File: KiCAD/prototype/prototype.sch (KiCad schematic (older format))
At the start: 0 parts

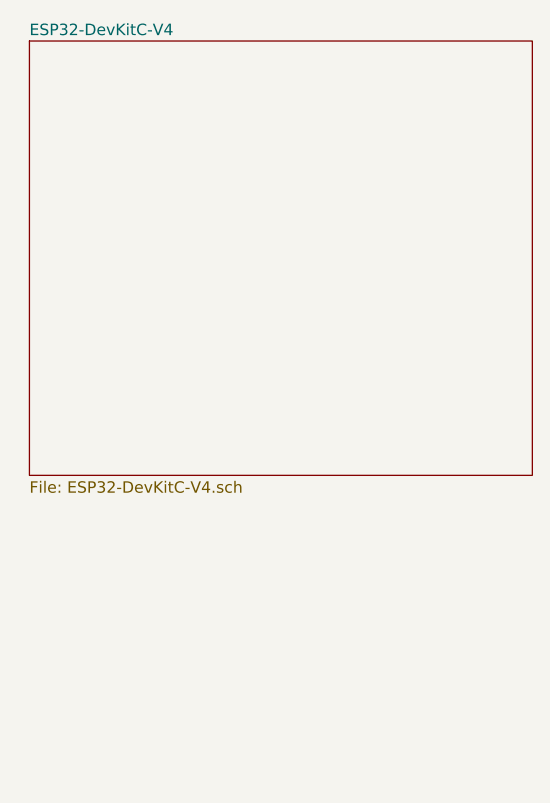
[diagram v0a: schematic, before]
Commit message: Export all signals to the schematic reference
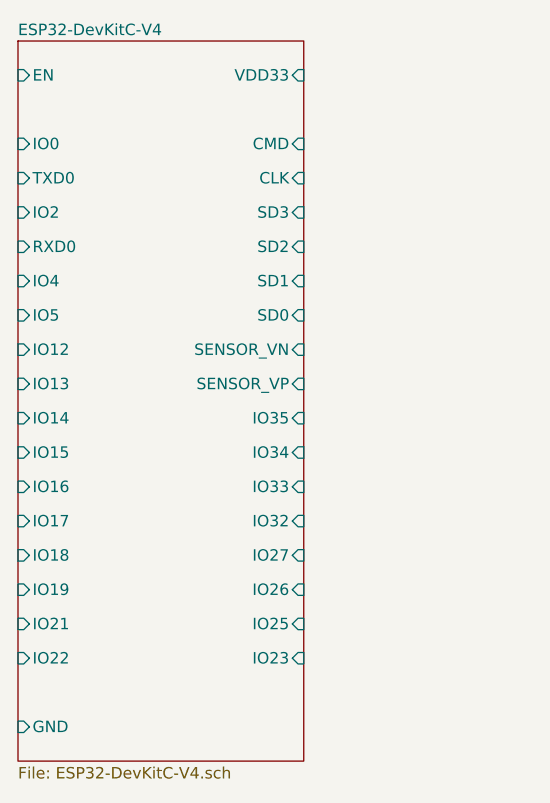
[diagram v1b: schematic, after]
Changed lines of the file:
@@
 $EndDescr
 $Sheet
-S 5150 2800 2200 1900
+S 5100 2800 1250 3150
 U 5F928E95
 F0 "ESP32-DevKitC-V4" 50
 F1 "ESP32-DevKitC-V4.sch" 50
+F2 "IO0" I L 5100 3250 50
+F3 "TXD0" I L 5100 3400 50
+F4 "IO2" I L 5100 3550 50
+F5 "RXD0" I L 5100 3700 50
+F6 "IO4" I L 5100 3850 50
+F7 "IO5" I L 5100 4000 50
+F8 "IO12" I L 5100 4150 50
+F9 "IO13" I L 5100 4300 50
+F10 "IO14" I L 5100 4450 50
+F11 "IO15" I L 5100 4600 50
+F12 "IO16" I L 5100 4750 50
+F13 "IO17" I L 5100 4900 50
+F14 "IO18" I L 5100 5050 50
+F15 "IO19" I L 5100 5200 50
+F16 "IO21" I L 5100 5350 50
+F17 "IO22" I L 5100 5500 50
+F18 "IO23" I R 6350 5500 50
+F19 "IO25" I R 6350 5350 50
+F20 "IO26" I R 6350 5200 50
+F21 "IO27" I R 6350 5050 50
+F22 "IO32" I R 6350 4900 50
+F23 "IO33" I R 6350 4750 50
+F24 "IO34" I R 6350 4600 50
+F25 "IO35" I R 6350 4450 50
+F26 "SENSOR_VP" I R 6350 4300 50
+F27 "SENSOR_VN" I R 6350 4150 50
+F28 "SD0" I R 6350 4000 50
+F29 "SD1" I R 6350 3850 50
+F30 "SD2" I R 6350 3700 50
+F31 "SD3" I R 6350 3550 50
+F32 "CLK" I R 6350 3400 50
+F33 "CMD" I R 6350 3250 50
+F34 "EN" I L 5100 2950 50
+F35 "VDD33" I R 6350 2950 50
+F36 "GND" I L 5100 5800 50
 $EndSheet
 $EndSCHEMATC

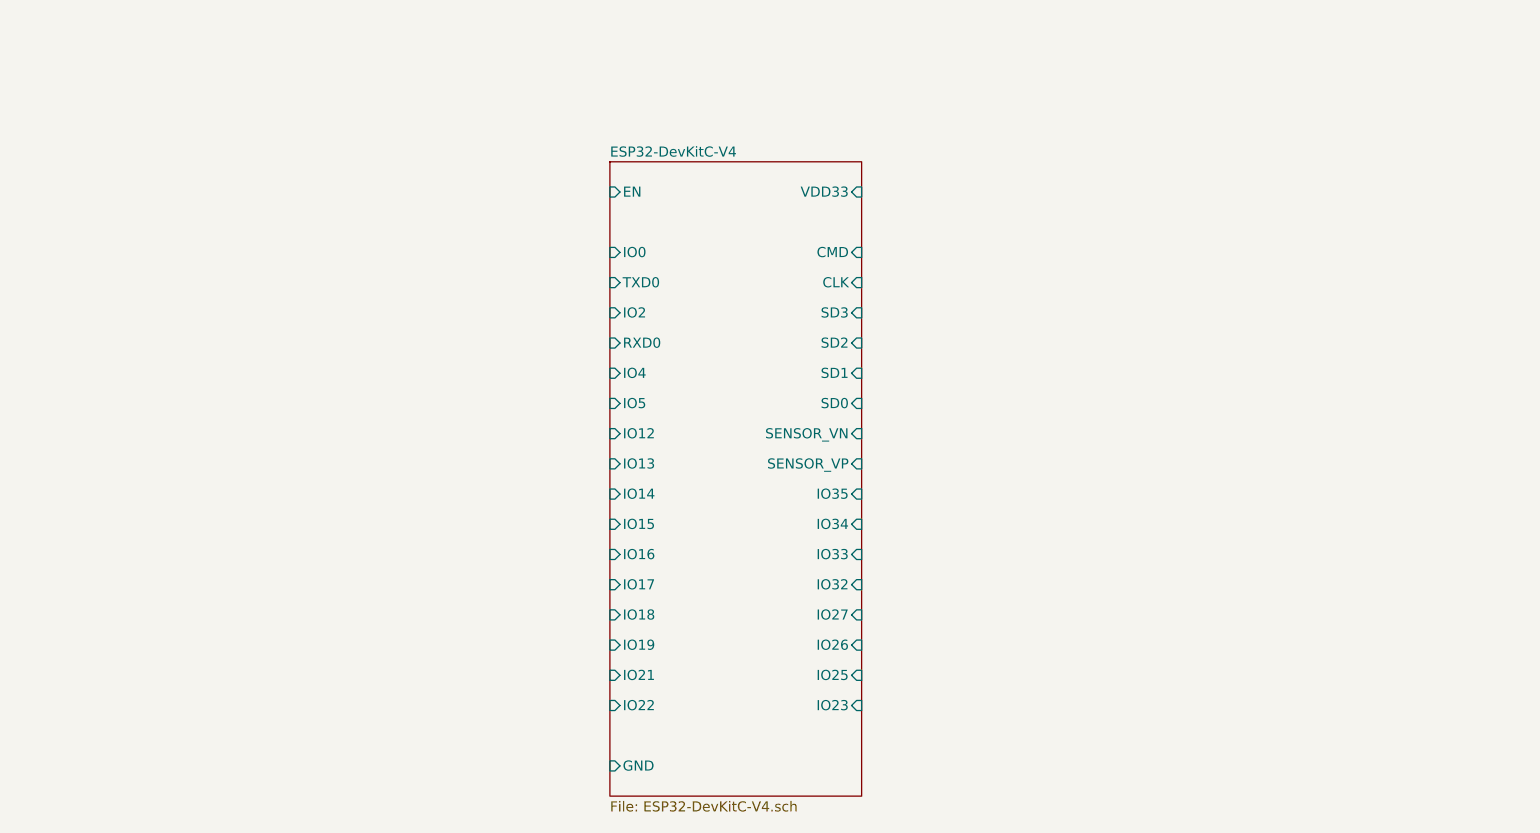
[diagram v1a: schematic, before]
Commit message: Correction of miss placed folder
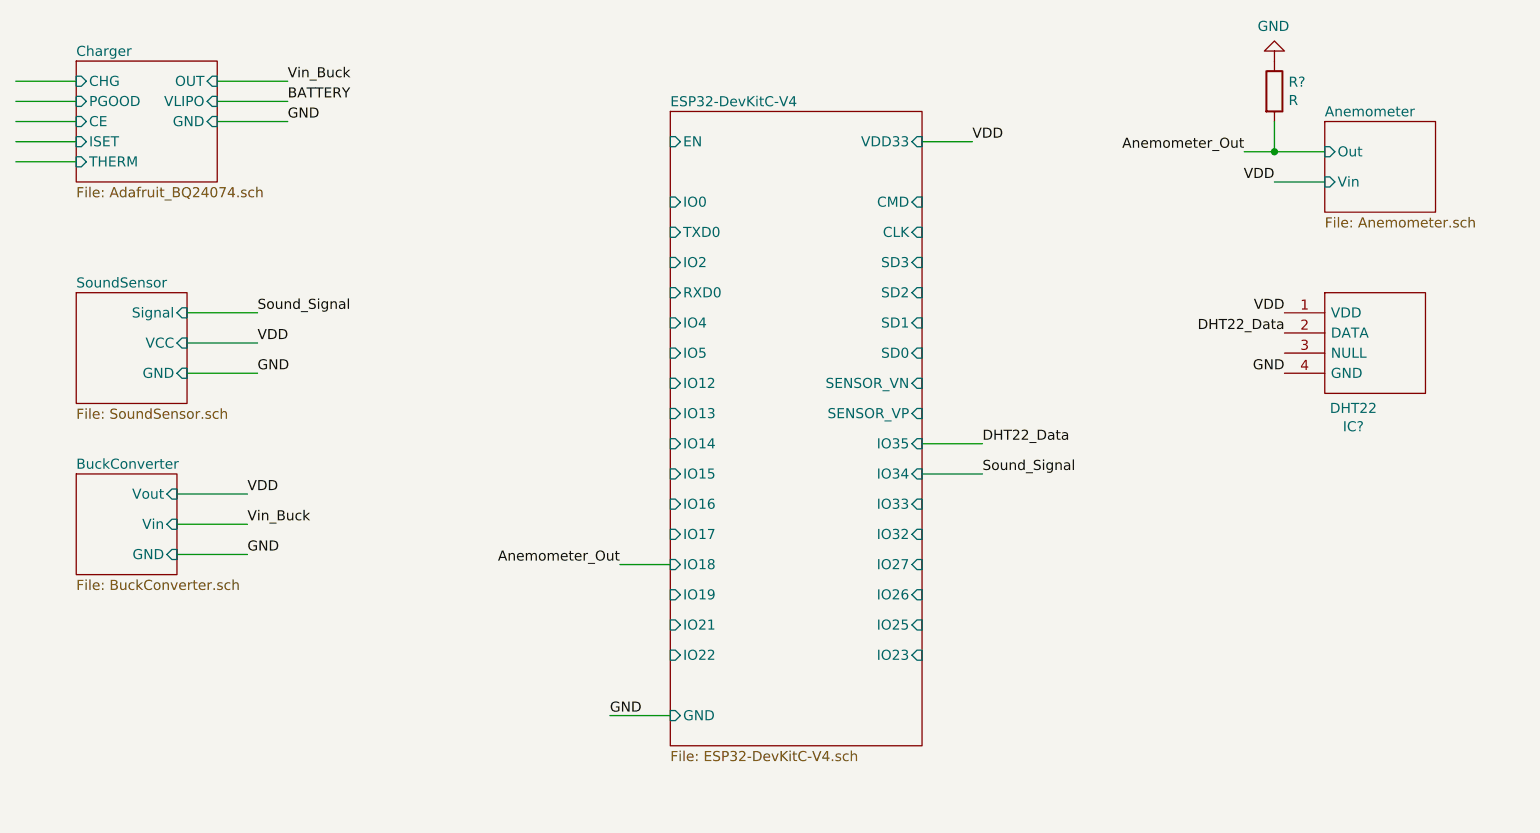
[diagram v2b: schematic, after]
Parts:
- added IC?: DHT22, DHT22, symbol DHT22:DHT22
- added R?: R, symbol Device:R
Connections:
- net labels added: Anemometer_Out, BATTERY, DHT22_Data, GND, Sound_Signal, VDD, Vin_Buck
- wire segments 0 -> 23
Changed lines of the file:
@@
 $Descr A4 11693 8268
 encoding utf-8
-Sheet 1 2
+Sheet 1 6
 Title "Software testing prototype schematics"
 Date "2020-10-22"
@@
 $EndDescr
 $Sheet
-S 5100 2800 1250 3150
+S 5400 2550 1250 3150
 U 5F928E95
 F0 "ESP32-DevKitC-V4" 50
 F1 "ESP32-DevKitC-V4.sch" 50
-F2 "IO0" I L 5100 3250 50
-F3 "TXD0" I L 5100 3400 50
-F4 "IO2" I L 5100 3550 50
-F5 "RXD0" I L 5100 3700 50
-F6 "IO4" I L 5100 3850 50
-F7 "IO5" I L 5100 4000 50
-F8 "IO12" I L 5100 4150 50
-F9 "IO13" I L 5100 4300 50
-F10 "IO14" I L 5100 4450 50
-F11 "IO15" I L 5100 4600 50
-F12 "IO16" I L 5100 4750 50
-F13 "IO17" I L 5100 4900 50
-F14 "IO18" I L 5100 5050 50
-F15 "IO19" I L 5100 5200 50
-F16 "IO21" I L 5100 5350 50
-F17 "IO22" I L 5100 5500 50
-F18 "IO23" I R 6350 5500 50
-F19 "IO25" I R 6350 5350 50
-F20 "IO26" I R 6350 5200 50
-F21 "IO27" I R 6350 5050 50
-F22 "IO32" I R 6350 4900 50
-F23 "IO33" I R 6350 4750 50
-F24 "IO34" I R 6350 4600 50
-F25 "IO35" I R 6350 4450 50
-F26 "SENSOR_VP" I R 6350 4300 50
-F27 "SENSOR_VN" I R 6350 4150 50
-F28 "SD0" I R 6350 4000 50
-F29 "SD1" I R 6350 3850 50
-F30 "SD2" I R 6350 3700 50
-F31 "SD3" I R 6350 3550 50
-F32 "CLK" I R 6350 3400 50
-F33 "CMD" I R 6350 3250 50
-F34 "EN" I L 5100 2950 50
-F35 "VDD33" I R 6350 2950 50
-F36 "GND" I L 5100 5800 50
-$EndSheet
+F2 "IO0" I L 5400 3000 50
+F3 "TXD0" I L 5400 3150 50
+F4 "IO2" I L 5400 3300 50
+F5 "RXD0" I L 5400 3450 50
+F6 "IO4" I L 5400 3600 50
+F7 "IO5" I L 5400 3750 50
+F8 "IO12" I L 5400 3900 50
+F9 "IO13" I L 5400 4050 50
+F10 "IO14" I L 5400 4200 50
+F11 "IO15" I L 5400 4350 50
+F12 "IO16" I L 5400 4500 50
+F13 "IO17" I L 5400 4650 50
+F14 "IO18" I L 5400 4800 50
+F15 "IO19" I L 5400 4950 50
+F16 "IO21" I L 5400 5100 50
+F17 "IO22" I L 5400 5250 50
+F18 "IO23" I R 6650 5250 50
+F19 "IO25" I R 6650 5100 50
+F20 "IO26" I R 6650 4950 50
+F21 "IO27" I R 6650 4800 50
+F22 "IO32" I R 6650 4650 50
+F23 "IO33" I R 6650 4500 50
+F24 "IO34" I R 6650 4350 50
+F25 "IO35" I R 6650 4200 50
+F26 "SENSOR_VP" I R 6650 4050 50
+F27 "SENSOR_VN" I R 6650 3900 50
+F28 "SD0" I R 6650 3750 50
+F29 "SD1" I R 6650 3600 50
+F30 "SD2" I R 6650 3450 50
+F31 "SD3" I R 6650 3300 50
+F32 "CLK" I R 6650 3150 50
+F33 "CMD" I R 6650 3000 50
+F34 "EN" I L 5400 2700 50
+F35 "VDD33" I R 6650 2700 50
+F36 "GND" I L 5400 5550 50
+$EndSheet
+$Sheet
+S 2450 3450 550  550
+U 5FAFBD3D
+F0 "SoundSensor" 50
+F1 "SoundSensor.sch" 50
+F2 "GND" I R 3000 3850 50
+F3 "VCC" I R 3000 3700 50
+F4 "Signal" I R 3000 3550 50
+$EndSheet
+$Sheet
+S 2450 4350 500  500
+U 5FB0CF58
+F0 "BuckConverter" 50
+F1 "BuckConverter.sch" 50
+F2 "Vin" I R 2950 4600 50
+F3 "Vout" I R 2950 4450 50
+F4 "GND" I R 2950 4750 50
+$EndSheet
+Wire Wire Line
+	6650 2700 6900 2700
+Wire Wire Line
+	3000 3700 3350 3700
+Text Label 3350 3700 0    50   ~ 0
+VDD
+Text Label 6900 2700 0    50   ~ 0
+VDD
+Wire Wire Line
+	2950 4450 3300 4450
+Text Label 3300 4450 0    50   ~ 0
+VDD
+Wire Wire Line
+	2950 4600 3300 4600
+Text Label 3300 4600 0    50   ~ 0
+Vin_Buck
+Wire Wire Line
+	3000 3850 3350 3850
+Wire Wire Line
+	2950 4750 3300 4750
+Wire Wire Line
+	5400 5550 5100 5550
+Text Label 5100 5550 0    50   ~ 0
+GND
+Text Label 3300 4750 0    50   ~ 0
+GND
+Text Label 3350 3850 0    50   ~ 0
+GND
+Wire Wire Line
+	3000 3550 3350 3550
+Text Label 3350 3550 0    50   ~ 0
+Sound_Signal
+Wire Wire Line
+	6650 4350 6950 4350
+Text Label 6950 4350 0    50   ~ 0
+Sound_Signal
+$Comp
+L DHT22:DHT22 IC?
+U 1 1 5FB3BE3A
+P 8450 3550
+F 0 "IC?" H 8792 2985 50  0000 C CNN
+F 1 "DHT22" H 8792 3076 50  0000 C CNN
+F 2 "DHT22" H 9200 3650 50  0001 L CNN
+F 3 "https://datasheet4u.com/datasheet-parts/DHT22-datasheet.php?id=792211" H 9200 3550 50  0001 L CNN
+F 4 "Digital-output relative humidity & temperature sensor/module DHT22" H 9200 3450 50  0001 L CNN "Description"
+F 5 "25.1" H 9200 3350 50  0001 L CNN "Height"
+F 6 "Aosong Electronics" H 9200 3250 50  0001 L CNN "Manufacturer_Name"
+F 7 "DHT22" H 9200 3150 50  0001 L CNN "Manufacturer_Part_Number"
+F 8 "" H 9200 3050 50  0001 L CNN "Arrow Part Number"
+F 9 "" H 9200 2950 50  0001 L CNN "Arrow Price/Stock"
+F 10 "" H 9200 2850 50  0001 L CNN "Mouser Part Number"
+F 11 "" H 9200 2750 50  0001 L CNN "Mouser Price/Stock"
+	1    8450 3550
+	1    0    0    -1
+$EndComp
+Text Label 8450 3850 2    50   ~ 0
+GND
+Text Label 8450 3550 2    50   ~ 0
+VDD
+Wire Wire Line
+	6650 4200 6950 4200
+Text Label 6950 4200 0    50   ~ 0
+DHT22_Data
+Text Label 8450 3650 2    50   ~ 0
+DHT22_Data
+$Sheet
+S 8650 2600 550  450
+U 5FB3DFB3
+F0 "Anemometer" 50
+F1 "Anemometer.sch" 50
+F2 "Vin" I L 8650 2900 50
+F3 "Out" I L 8650 2750 50
+$EndSheet
+Wire Wire Line
+	8650 2750 8400 2750
+Wire Wire Line
+	8650 2900 8400 2900
+Wire Wire Line
+	8400 2750 8400 2600
+$Comp
+L Device:R R?
+U 1 1 5FB40072
+P 8400 2450
+F 0 "R?" H 8470 2496 50  0000 L CNN
+F 1 "R" H 8470 2405 50  0000 L CNN
+F 2 "" V 8330 2450 50  0001 C CNN
+F 3 "~" H 8400 2450 50  0001 C CNN
+	1    8400 2450
+	1    0    0    -1
+$EndComp
+$Comp
+L power:GND #PWR?
+U 1 1 5FB404F7
+P 8400 2300
+F 0 "#PWR?" H 8400 2050 50  0001 C CNN
+F 1 "GND" H 8405 2127 50  0000 C CNN
+F 2 "" H 8400 2300 50  0001 C CNN
+F 3 "" H 8400 2300 50  0001 C CNN
+	1    8400 2300
+	-1   0    0    1
+$EndComp
+Wire Wire Line
+	8400 2750 8250 2750
+Connection ~ 8400 2750
+Text Label 8400 2900 2    50   ~ 0
+VDD
+Text Label 8250 2750 2    50   ~ 0
+Anemometer_Out
+Wire Wire Line
+	5400 4800 5150 4800
+Text Label 5150 4800 2    50   ~ 0
+Anemometer_Out
+$Sheet
+S 2450 2300 700  600
+U 5FB60B8D
+F0 "Charger" 50
+F1 "Adafruit_BQ24074.sch" 50
+F2 "THERM" I L 2450 2800 50
+F3 "ISET" I L 2450 2700 50
+F4 "CE" I L 2450 2600 50
+F5 "PGOOD" I L 2450 2500 50
+F6 "CHG" I L 2450 2400 50
+F7 "OUT" I R 3150 2400 50
+F8 "VLIPO" I R 3150 2500 50
+F9 "GND" I R 3150 2600 50
+$EndSheet
+Wire Wire Line
+	3150 2400 3500 2400
+Wire Wire Line
+	3150 2500 3500 2500
+Wire Wire Line
+	3150 2600 3500 2600
+Wire Wire Line
+	2450 2400 2150 2400
+Wire Wire Line
+	2450 2500 2150 2500
+Wire Wire Line
+	2450 2600 2150 2600
+Wire Wire Line
+	2450 2700 2150 2700
+Wire Wire Line
+	2450 2800 2150 2800
+Text Label 3500 2400 0    50   ~ 0
+Vin_Buck
+Text Label 3500 2600 0    50   ~ 0
+GND
+Text Label 3500 2500 0    50   ~ 0
+BATTERY
 $EndSCHEMATC

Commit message: Improve Anemometer schematics
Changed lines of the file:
@@
 F0 "Anemometer" 50
 F1 "Anemometer.sch" 50
-F2 "Vin" I L 8650 2900 50
-F3 "Out" I L 8650 2750 50
+F2 "Out" I L 8650 2750 50
+F3 "COM" I L 8650 2900 50
 $EndSheet
 Wire Wire Line
